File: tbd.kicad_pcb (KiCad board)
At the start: 2 copper layers, 22.6 x 12 mm, 8 parts, among them J1 USBPCB, P1 CONN_02X04, U1 MKL27ZxxxVFM4

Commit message: Update design to v0.2
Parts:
- added J2: USB-MICROB-5PIN, tbd:SparkFun-USB-MICROB, B.Cu at (107.9, 94.8)
- added R3: 33R, tbd:R_0603, B.Cu at (119.3, 98.6)
- added SWD_CLK: SWD_CLK, Measurement_Points:Measurement_Point_Round-SMD-Pad_Small, B.Cu at (116.0, 94.8)
- C1, C2: footprint tbd:SparkFun-0402-CAP -> tbd:C_0603
- LED1: footprint tbd:SparkFun-LED-0402 -> tbd:LED-0603
- P1: footprint tbd:hdr-boardedge-4x2 -> tbd:HEADER_2x4_SMT_RA
- R1: value 33R -> 100R; footprint tbd:SparkFun-0402-RES -> tbd:R_0603
- R2: footprint tbd:SparkFun-0402-RES -> tbd:R_0603
- moved C2 10.2 mm to (116.2, 90.9), turned to 90 degrees
- moved R2 9.57 mm to (119.3, 99.8)
- moved P1 9.27 mm to (117.6, 91.1), turned to 90 degrees
- moved R1 8.71 mm to (122.5, 98.8), turned to 270 degrees
- moved LED1 8.08 mm to (124.6, 97.3), turned to 90 degrees
- moved C1 6.35 mm to (117.3, 97.1), turned to 180 degrees
- moved U1 3.58 mm to (119.9, 93.3), turned to 90 degrees
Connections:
- LED1 pad A: +3.3V -> Net-(LED1-PadA)
- P1 pad 1: LPUART0_RX -> +3.3V
- P1 pad 2: SWD_CLK -> SPI1_SS
- P1 pad 3: LPUART0_TX -> I2C1_SDA
- P1 pad 4: SWD_DIO -> SPI1_SCK
- P1 pad 5: /RESET -> I2C1_SCL
- P1 pad 6: /NMI -> SPI1_MOSI
- P1 pad 8: VSS -> SPI1_MISO
- R1 pad 1: Net-(J1-PadDP) -> +3.3V
- R1 pad 2: Net-(R1-Pad2) -> Net-(LED1-PadA)
- R2 pad 1: Net-(J1-PadDN) -> Net-(J1-PadDP)
- U1 pad 10: SWD_CLK -> Net-(TP1-Pad1)
- U1 pad 11: LPUART0_RX -> (no net)
- U1 pad 12: LPUART0_TX -> (no net)
- U1 pad 13: SWD_DIO -> I2C1_SCL
- U1 pad 14: /NMI -> I2C1_SDA
- U1 pad 19: /RESET -> (no net)
- U1 pad 29: (no net) -> SPI1_SS
- U1 pad 3: Net-(R1-Pad2) -> Net-(R2-Pad2)
- U1 pad 30: (no net) -> SPI1_SCK
- U1 pad 31: (no net) -> SPI1_MOSI
- U1 pad 32: (no net) -> SPI1_MISO
- U1 pad 4: Net-(R2-Pad2) -> Net-(R3-Pad2)
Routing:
- net Net-(LED1-PadC): track 24.1 -> 3.23 mm
- net /RESET: track 16.9 -> 0.00 mm, vias 1 -> 0
- net SWD_DIO: track 11.6 -> 0.00 mm
- net LPUART0_RX: track 10.2 -> 0.00 mm, vias 1 -> 0
- net SWD_CLK: track 8.55 -> 0.00 mm
- net LPUART0_TX: track 7.68 -> 0.00 mm, vias 1 -> 0
- net I2C1_SCL: track 0.00 -> 6.63 mm, vias 0 -> 1
- net SPI1_MISO: track 0.00 -> 6.38 mm, vias 0 -> 1
- net Net-(J1-PadDP): track 17.9 -> 23.7 mm, vias 1 -> 2
- net /NMI: track 5.43 -> 0.00 mm
- net SPI1_SS: track 0.00 -> 4.35 mm, vias 0 -> 1
- net SPI1_MOSI: track 0.00 -> 3.98 mm, vias 0 -> 1
- net Net-(R3-Pad2): track 0.00 -> 3.95 mm
- net VSS: track 65.4 -> 69.2 mm, vias 5 -> 14
- net SPI1_SCK: track 0.00 -> 3.51 mm, vias 0 -> 1
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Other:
- board size 22.6 x 12 mm -> 20.3 x 12 mm
- net class pwr added: clearance 0.127, trace_width 0.508, via_dia 0.6858, via_drill 0.3302
- board text added: "3.3V"
- board text added: "GND"
- board text added: "I2C1_SCK"
- board text added: "I2C1_SDA"
- board text added: "SPI1_MISO"
- board text added: "SPI1_MOSI"
- board text added: "SPI1_SCK"
- board text added: "SPI1_SS"
- board text added: "T B D"
- board text added: "V 0 . 2"
- board text removed: "1"
- board text removed: "TBD MKL27Z256VFM4 v0.1 a.litt"

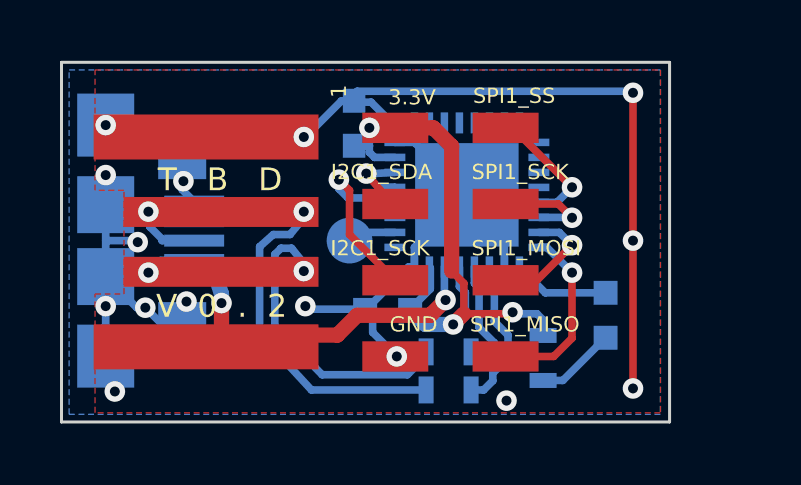
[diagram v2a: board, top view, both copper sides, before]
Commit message: Add OSHW logo, clean up silk
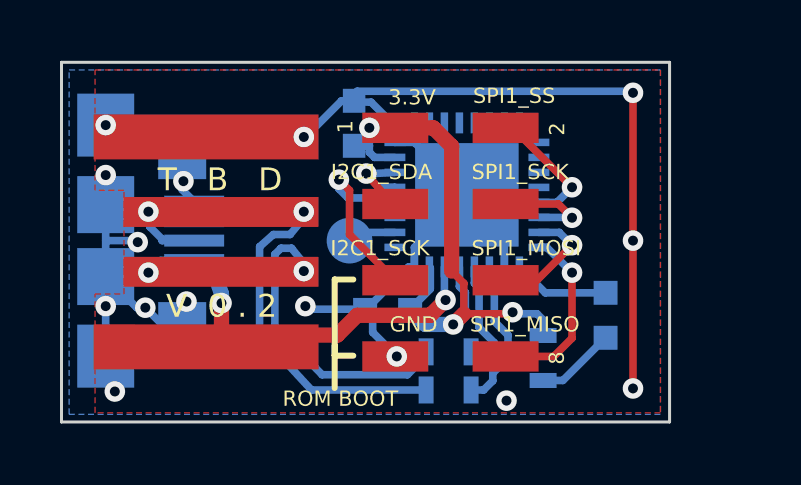
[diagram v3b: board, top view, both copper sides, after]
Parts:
- added G***: LOGO, tbd:OSHW_LOGO_NOTEXT_TINY, B.Cu at (113.8, 98.5)
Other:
- board text added: "1"
- board text added: "2"
- board text added: "8"
- board text added: "ROM BOOT"

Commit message: Stitch ground plane near USB resistors, hackaday.io URL as board ID, add port IDs to pins and LED
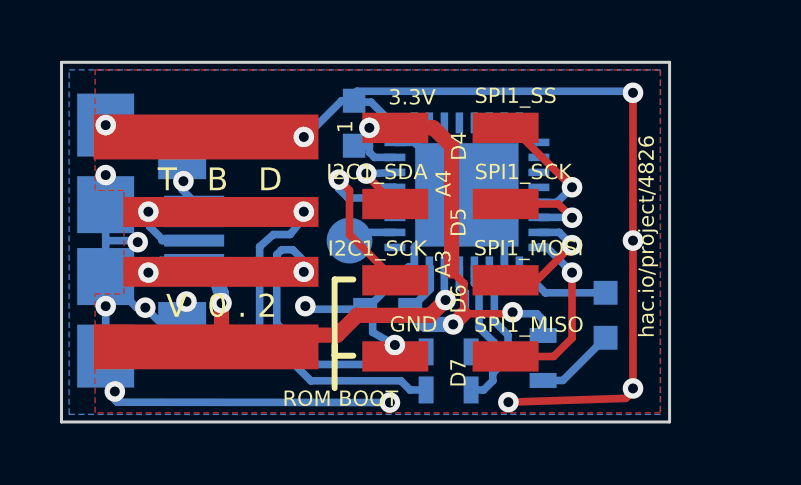
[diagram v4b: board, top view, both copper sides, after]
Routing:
- net VSS: track 69.2 -> 82.7 mm, vias 14 -> 16
- net Net-(J1-PadDN): track 19.6 -> 21.9 mm
- net (no net): vias 1 -> 0
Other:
- board text added: "A3"
- board text added: "A4"
- board text added: "D4"
- board text added: "D5"
- board text added: "D6"
- board text added: "D7"
- board text added: "E0"
- board text added: "hac.io/project/4826"
- board text removed: "2"
- board text removed: "8"
